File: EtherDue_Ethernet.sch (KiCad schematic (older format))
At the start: 32 parts, among them Q201 2N7002, U201 W5100, U202 APX811, U203 HY931147C, X201 25MHz

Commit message: Final ERC cleanup, export net file
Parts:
- added U602: SJ, symbol SJ
- U603: renamed from U202; value APX811 -> APX811-44UG-7
- renumbered C201 to C601, C202 to C602, C203 to C603, C204 to C604, C205 to C605, C206 to C606, C207 to C607, C208 to C608, C209 to C609, C210 to C610, C211 to C611, D201 to D601, D202 to D602, D203 to D603, D204 to D604, D205 to D605, D206 to D606, JP201 to JP601, JP202 to JP602, L201 to L601, L202 to L602, Q201 to Q601, R201 to R601, R202 to R602, R203 to R603, R204 to R604, R205 to R605, R206 to R606, U201 to U601, U203 to U604, X201 to X601
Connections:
- wire segments 144 -> 145
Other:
- note added: "/SCS & SS0 Behaviour:\n\nMISO pin tri-state\nby SS & /SCS\n\nSS0 low\nsimultaneously\ndrives SEN high\n-> SPI enabled\n& chip selected"
- note added: "Reset IC - 140ms min, 280ms max\n< 4.38 Vrst, push-pull output"
- note added: "This jumper is just to\nkeep Kicad's default\nERC rules happy\n(disallows direct\nBidi <->Power\nconnections)"
- note removed: "nCS Behaviour:\n\nMISO pin tri-state\nby SS & /CS\n\n/CS low\nsimultaneously\nSEN high\n= SPI enabled\n& chip selected"

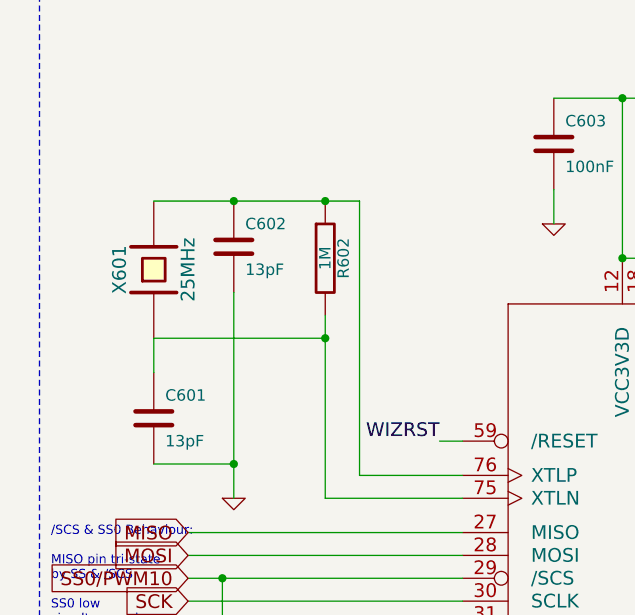
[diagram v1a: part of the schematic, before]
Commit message: Change Ethernet Crystal to a KX-7, load capacitors to match
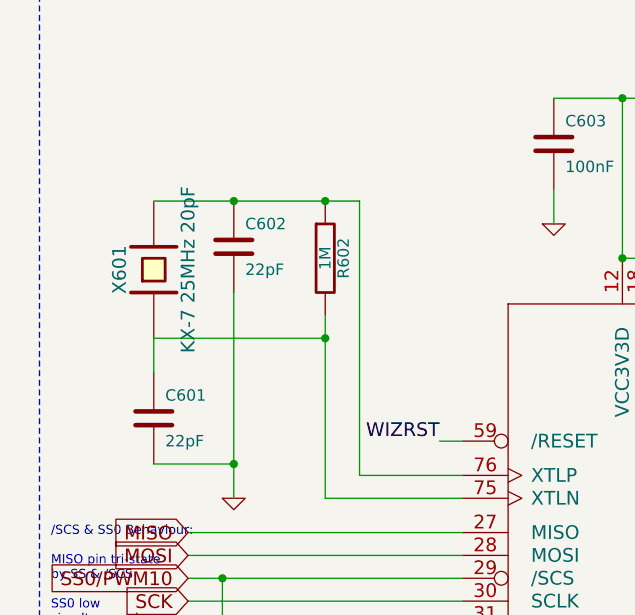
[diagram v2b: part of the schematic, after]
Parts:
- C601, C602: value 13pF -> 22pF
- X601: value 25MHz -> KX-7 25MHz 20pF
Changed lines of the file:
@@
-EESchema Schematic File Version 2  date Thu 11 Apr 2013 16:32:55 EST
+EESchema Schematic File Version 2  date Fri 03 May 2013 10:36:30 EST
 LIBS:power
 LIBS:device
@@
 Sheet 6 6
 Title ""
-Date "11 apr 2013"
+Date "3 may 2013"
 Rev ""
 Comp ""
@@
 P 1350 1850
 F 0 "C602" H 1400 1950 50  0000 L CNN
-F 1 "13pF" H 1400 1750 50  0000 L CNN
+F 1 "22pF" H 1400 1750 50  0000 L CNN
 F 2 "" H 1350 1850 60  0001 C CNN
 F 3 "" H 1350 1850 60  0001 C CNN
@@
 P 1000 2600
 F 0 "C601" H 1050 2700 50  0000 L CNN
-F 1 "13pF" H 1050 2500 50  0000 L CNN
+F 1 "22pF" H 1050 2500 50  0000 L CNN
 F 2 "" H 1000 2600 60  0001 C CNN
 F 3 "" H 1000 2600 60  0001 C CNN
@@
 P 1000 1950
 F 0 "X601" H 1000 2100 60  0000 C CNN
-F 1 "25MHz" H 1000 1800 60  0000 C CNN
+F 1 "KX-7 25MHz 20pF" H 1000 1800 60  0000 C CNN
 F 2 "" H 1000 1950 60  0001 C CNN
 F 3 "" H 1000 1950 60  0001 C CNN

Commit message: Edit pass of footprints, cleanup symbols, etc.
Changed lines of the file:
@@
-EESchema Schematic File Version 2  date Fri 03 May 2013 10:36:30 EST
+EESchema Schematic File Version 2  date Fri 03 May 2013 15:34:29 EST
+LIBS:freetronics_kicad_sch_lib
 LIBS:power
 LIBS:device
@@
 LIBS:contrib
 LIBS:valves
-LIBS:freetronics_kicad_sch_lib
 LIBS:EtherDue-cache
 EELAYER 24 0
@@
 U 1 1 51663ACC
 P 5500 6600
-F 0 "L602" V 5450 6600 40  0000 C CNN
-F 1 "1uH 250mA" V 5600 6600 40  0000 C CNN
+F 0 "L602" H 5450 6700 40  0000 C CNN
+F 1 "1uH 250mA" H 5500 6550 40  0000 C CNN
 F 2 "" H 5500 6600 60  0001 C CNN
 F 3 "" H 5500 6600 60  0001 C CNN
 	1    5500 6600
-	0    -1   -1   0
+	1    0    0    -1
 $EndComp
 $Comp
@@
 U 1 1 51663A74
 P 3500 6600
-F 0 "L601" V 3450 6600 40  0000 C CNN
-F 1 "1uH 250mA" V 3600 6600 40  0000 C CNN
+F 0 "L601" H 3500 6550 40  0000 C CNN
+F 1 "1uH 250mA" H 3500 6700 40  0000 C CNN
 F 2 "" H 3500 6600 60  0001 C CNN
 F 3 "" H 3500 6600 60  0001 C CNN
 	1    3500 6600
-	0    -1   -1   0
-$EndComp
-$Comp
+	1    0    0    -1
+$EndComp
+$Comp

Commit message: General clean up, component selection, etc.
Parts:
- removed JP602: D2_INT, symbol JUMPER
- removed U602: SJ, symbol SJ
- added SJ601: SJ, ~, symbol SJ
- renumbered U601 to IC601
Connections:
- net labels added: (Open by default)
- wire segments 145 -> 144
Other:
- note removed: "This jumper is just to\nkeep Kicad's default\nERC rules happy\n(disallows direct\nBidi <->Power\nconnections)"
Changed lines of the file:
@@
-EESchema Schematic File Version 2  date Fri 03 May 2013 15:34:29 EST
+EESchema Schematic File Version 2  date Tue 04 Jun 2013 15:53:49 EST
 LIBS:freetronics_kicad_sch_lib
 LIBS:power
@@
 Sheet 6 6
 Title ""
-Date "3 may 2013"
+Date "4 jun 2013"
 Rev ""
 Comp ""
@@
 	1650 3500 2350 3500
 Wire Wire Line
-	1000 5450 1400 5450
+	1000 5450 1500 5450
 Wire Wire Line
 	1950 5950 2200 5950
@@
 	5750 3800 5750 4000
 Wire Wire Line
-	5150 5100 5150 5200
+	5150 5100 5150 5650
 Wire Wire Line
 	4450 5100 5150 5100
@@
 	2200 3800 2200 5950
 Wire Wire Line
-	2000 5450 2050 5450
+	1900 5450 2050 5450
 Wire Wire Line
 	2050 5450 2050 3650
@@
 PWM2
 $Comp
-L JUMPER JP602
-U 1 1 51661DAE
-P 1700 5450
-F 0 "JP602" H 1700 5600 60  0000 C CNN
-F 1 "D2_INT" H 1700 5370 40  0000 C CNN
-F 2 "" H 1700 5450 60  0001 C CNN
-F 3 "" H 1700 5450 60  0001 C CNN
-	1    1700 5450
-	-1   0    0    1
-$EndComp
-$Comp
 L GND #PWR097
 U 1 1 51661CDB
@@
 $EndComp
 $Comp
-L W5100 U601
+L W5100 IC601
 U 1 1 51661783
 P 3950 3550
-F 0 "U601" H 2450 1950 70  0000 C BNN
+F 0 "IC601" H 2450 1950 70  0000 C BNN
 F 1 "W5100" H 2500 2050 70  0000 C BNN
 F 2 "" H 3950 3550 60  0001 C CNN
@@
 Wire Wire Line
 	8200 7000 8000 7000
-$Comp
-L SJ U602
-U 1 1 516662EA
-P 5150 5400
-F 0 "U602" H 5050 5250 70  0000 L BNN
-F 1 "SJ" H 5050 5500 70  0000 L BNN
-F 2 "" H 5150 5400 60  0000 C CNN
-F 3 "" H 5150 5400 60  0000 C CNN
-	1    5150 5400
-	0    -1   -1   0
-$EndComp
-Wire Wire Line
-	5150 5650 5150 5600
-Text Notes 5350 5300 0    39   ~ 0
-This jumper is just to\nkeep Kicad's default\nERC rules happy\n(disallows direct\nBidi <->Power\nconnections)
 Text Notes 8450 6700 0    40   ~ 0
 Reset IC - 140ms min, 280ms max\n< 4.38 Vrst, push-pull output
+$Comp
+L SJ SJ601
+U 1 1 51AD89B9
+P 1700 5450
+F 0 "SJ601" H 1600 5300 70  0000 L BNN
+F 1 "SJ" H 1600 5550 70  0001 L BNN
+F 2 "~" H 1700 5450 60  0000 C CNN
+F 3 "~" H 1700 5450 60  0000 C CNN
+	1    1700 5450
+	1    0    0    -1
+$EndComp
+Text Label 1250 5400 0    60   ~ 0
+(Open by default)
 $EndSCHEMATC

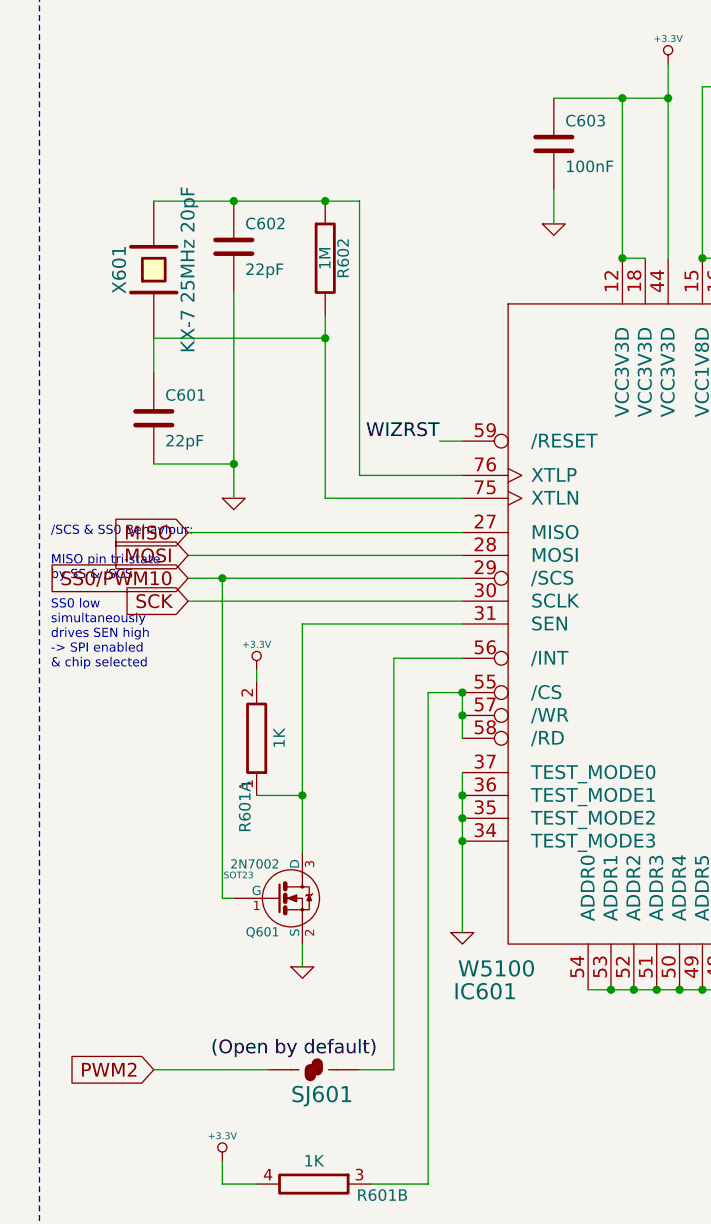
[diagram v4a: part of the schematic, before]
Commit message: Footprints checked, components imported to board but most not placed
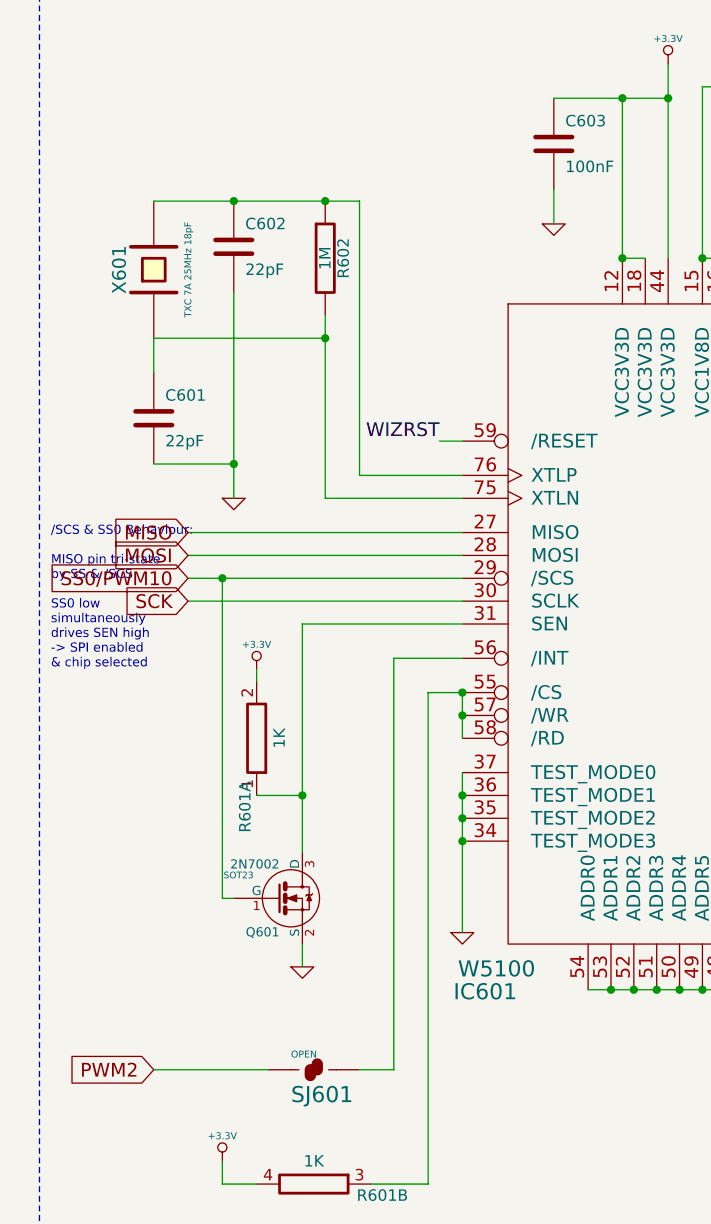
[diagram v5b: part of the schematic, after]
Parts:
- SJ601: value SJ -> OPEN
- X601: value KX-7 25MHz 20pF -> TXC 7A 25MHz 18pF
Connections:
- net labels removed: (Open by default)
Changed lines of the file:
@@
-EESchema Schematic File Version 2  date Tue 04 Jun 2013 15:53:49 EST
+EESchema Schematic File Version 2  date Thu 06 Jun 2013 09:35:07 EST
 LIBS:freetronics_kicad_sch_lib
 LIBS:power
@@
 Sheet 6 6
 Title ""
-Date "4 jun 2013"
+Date "5 jun 2013"
 Rev ""
 Comp ""
@@
 P 1000 1950
 F 0 "X601" H 1000 2100 60  0000 C CNN
-F 1 "KX-7 25MHz 20pF" H 1000 1800 60  0000 C CNN
+F 1 "TXC 7A 25MHz 18pF" H 1000 1800 30  0000 C CNN
 F 2 "" H 1000 1950 60  0001 C CNN
 F 3 "" H 1000 1950 60  0001 C CNN
@@
 P 1700 5450
 F 0 "SJ601" H 1600 5300 70  0000 L BNN
-F 1 "SJ" H 1600 5550 70  0001 L BNN
+F 1 "OPEN" H 1600 5500 30  0000 L BNN
 F 2 "~" H 1700 5450 60  0000 C CNN
 F 3 "~" H 1700 5450 60  0000 C CNN
@@
 	1    0    0    -1
 $EndComp
-Text Label 1250 5400 0    60   ~ 0
-(Open by default)
 $EndSCHEMATC
